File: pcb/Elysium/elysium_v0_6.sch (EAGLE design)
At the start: 20 parts, among them U1 TLC5940-NT, U2 TLC5940-NT, U3 TLC5940-NT, U4 TLC5940-NT, X1 5566-20

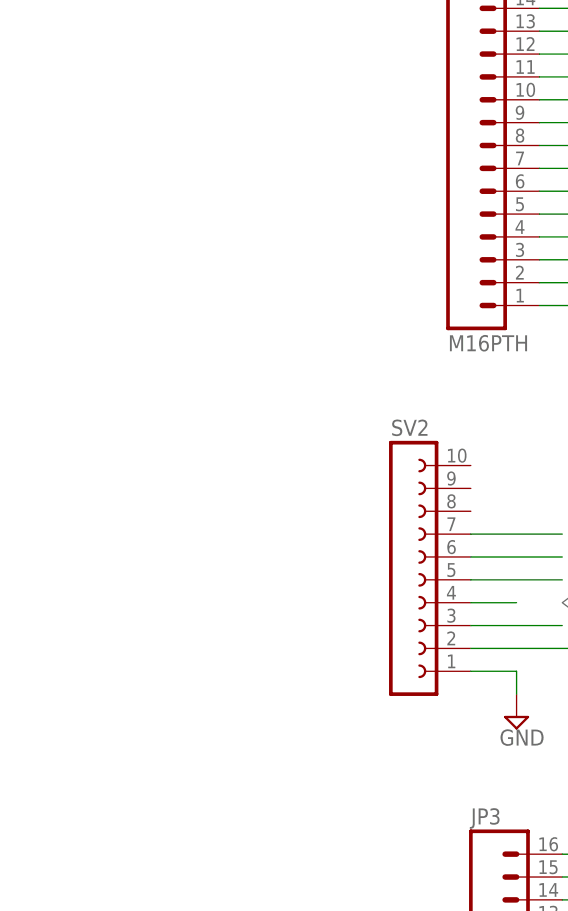
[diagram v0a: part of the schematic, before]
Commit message: Added mounting holes to v0.6 PCB.
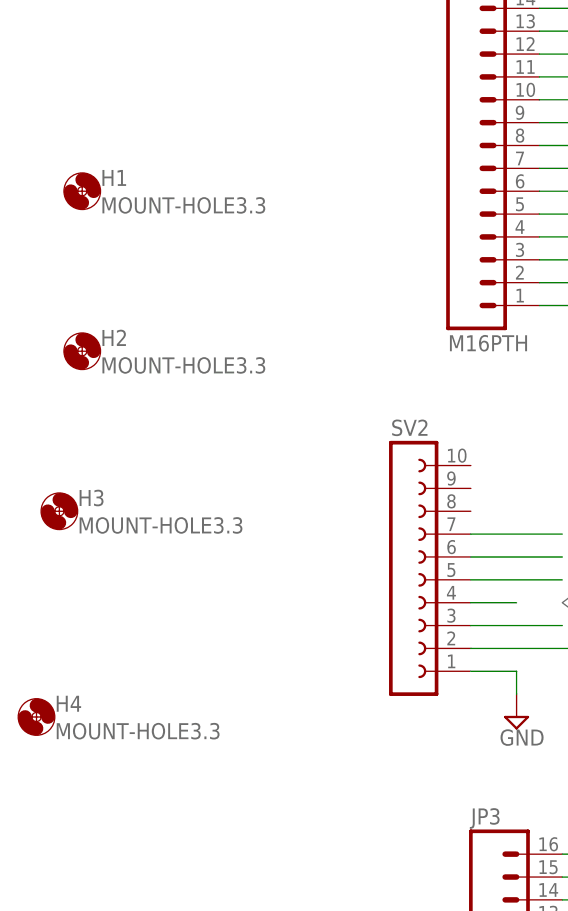
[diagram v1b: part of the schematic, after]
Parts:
- added H1, H2, H3, H4: MOUNT-HOLE3.3, holes:MOUNT-HOLE3.3
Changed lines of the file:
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@@
 <part name="SV2" library="con-lsta" deviceset="FE10-1" device=""/>
 <part name="SUPPLY1" library="supply2" deviceset="GND" device=""/>
+<part name="H1" library="holes" deviceset="MOUNT-HOLE" device="3.3"/>
+<part name="H2" library="holes" deviceset="MOUNT-HOLE" device="3.3"/>
+<part name="H3" library="holes" deviceset="MOUNT-HOLE" device="3.3"/>
+<part name="H4" library="holes" deviceset="MOUNT-HOLE" device="3.3"/>
 </parts>
 <sheets>
@@
 <instance part="SV2" gate="G$1" x="-15.24" y="10.16"/>
 <instance part="SUPPLY1" gate="GND" x="-2.54" y="-5.08"/>
+<instance part="H1" gate="G$1" x="-50.8" y="53.34"/>
+<instance part="H2" gate="G$1" x="-50.8" y="35.56"/>
+<instance part="H3" gate="G$1" x="-53.34" y="17.78"/>
+<instance part="H4" gate="G$1" x="-55.88" y="-5.08"/>
 </instances>
 <busses>
